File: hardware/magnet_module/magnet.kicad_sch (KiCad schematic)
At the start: 5 parts, among them U2 Leaf_Logo

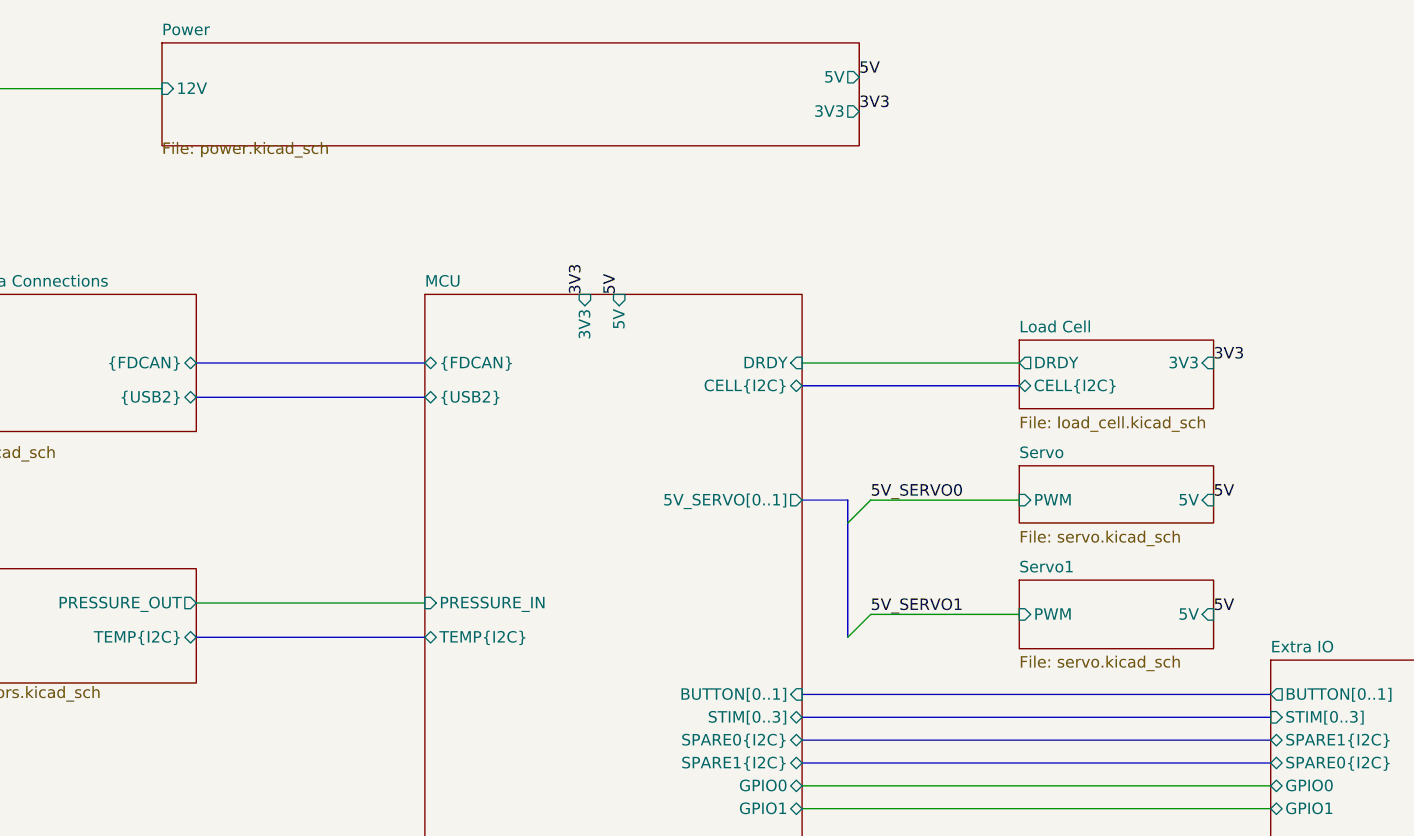
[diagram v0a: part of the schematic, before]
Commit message: change power LED brightness, move level shifter to servo page
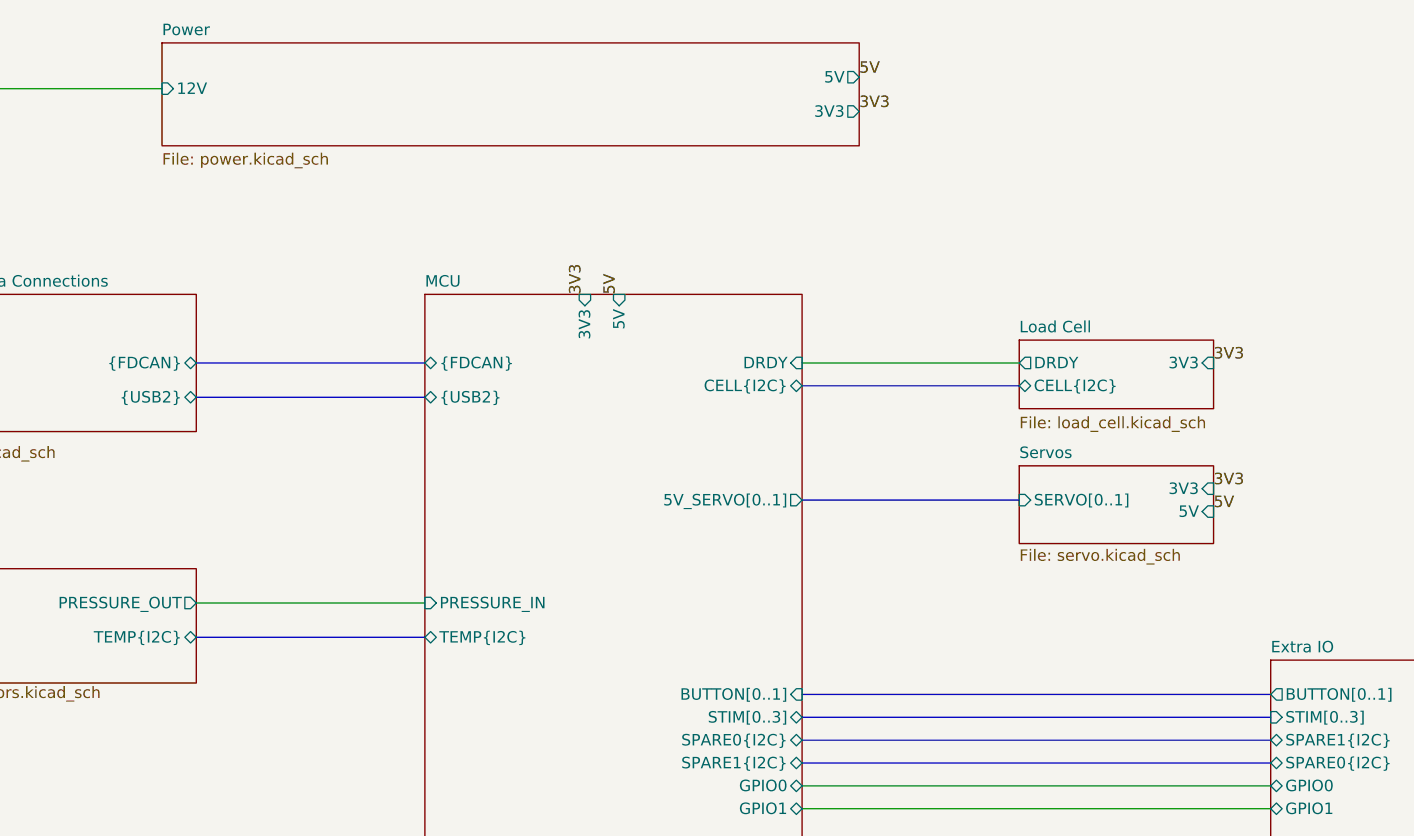
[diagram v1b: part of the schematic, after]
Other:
- sheet Servo renamed Servos
- removed sheet Servo1
- sheet Servos ports: added 3V3, SERVO[0..1]; removed PWM
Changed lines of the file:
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@@
 		(comment 1 "Prepared by LeafLabs, LLC")
 	)
-	(bus_entry
-		(at 176.53 104.14)
-		(size -2.54 2.54)
-		(stroke
-			(width 0)
-			(type default)
-		)
-	)
-	(bus_entry
-		(at 176.53 91.44)
-		(size -2.54 2.54)
+	(bus
+		(pts
+			(xy 168.91 91.44) (xy 193.04 91.44)
+		)
 		(stroke
 			(width 0)
@@
 	(bus
 		(pts
-			(xy 173.99 93.98) (xy 173.99 106.68)
+			(xy 168.91 113.03) (xy 220.98 113.03)
+		)
+		(stroke
+			(width 0)
+			(type default)
+		)
+	)
+	(bus
+		(pts
+			(xy 168.91 120.65) (xy 220.98 120.65)
 		)
 		(stroke
@@
 	(wire
 		(pts
-			(xy 176.53 104.14) (xy 193.04 104.14)
+			(xy 168.91 125.73) (xy 220.98 125.73)
 		)
 		(stroke
@@
 	(bus
 		(pts
-			(xy 168.91 113.03) (xy 220.98 113.03)
+			(xy 168.91 78.74) (xy 193.04 78.74)
+		)
+		(stroke
+			(width 0)
+			(type default)
+		)
+	)
+	(wire
+		(pts
+			(xy 36.83 176.53) (xy 34.29 176.53)
 		)
 		(stroke
@@
 	(bus
 		(pts
-			(xy 168.91 120.65) (xy 220.98 120.65)
+			(xy 168.91 118.11) (xy 220.98 118.11)
 		)
 		(stroke
@@
 	(wire
 		(pts
-			(xy 168.91 125.73) (xy 220.98 125.73)
+			(xy 68.58 72.39) (xy 60.96 72.39)
+		)
+		(stroke
+			(width 0)
+			(type default)
+		)
+	)
+	(wire
+		(pts
+			(xy 168.91 123.19) (xy 220.98 123.19)
+		)
+		(stroke
+			(width 0)
+			(type default)
+		)
+	)
+	(wire
+		(pts
+			(xy 60.96 45.72) (xy 97.79 45.72)
 		)
 		(stroke
@@
 	(bus
 		(pts
-			(xy 168.91 78.74) (xy 193.04 78.74)
-		)
-		(stroke
-			(width 0)
-			(type default)
-		)
-	)
-	(wire
-		(pts
-			(xy 36.83 176.53) (xy 34.29 176.53)
-		)
-		(stroke
-			(width 0)
-			(type default)
-		)
-	)
-	(bus
-		(pts
-			(xy 168.91 118.11) (xy 220.98 118.11)
-		)
-		(stroke
-			(width 0)
-			(type default)
-		)
-	)
-	(wire
-		(pts
-			(xy 68.58 72.39) (xy 60.96 72.39)
-		)
-		(stroke
-			(width 0)
-			(type default)
-		)
-	)
-	(bus
-		(pts
-			(xy 173.99 91.44) (xy 173.99 93.98)
-		)
-		(stroke
-			(width 0)
-			(type default)
-		)
-	)
-	(wire
-		(pts
-			(xy 168.91 123.19) (xy 220.98 123.19)
-		)
-		(stroke
-			(width 0)
-			(type default)
-		)
-	)
-	(wire
-		(pts
-			(xy 60.96 45.72) (xy 97.79 45.72)
-		)
-		(stroke
-			(width 0)
-			(type default)
-		)
-	)
-	(bus
-		(pts
-			(xy 168.91 91.44) (xy 173.99 91.44)
-		)
-		(stroke
-			(width 0)
-			(type default)
-		)
-	)
-	(bus
-		(pts
 			(xy 101.6 76.2) (xy 127 76.2)
-		)
-		(stroke
-			(width 0)
-			(type default)
-		)
-	)
-	(wire
-		(pts
-			(xy 176.53 91.44) (xy 193.04 91.44)
 		)
 		(stroke
@@
 		)
 	)
-	(label "5V_SERVO0"
-		(at 176.53 91.44 0)
+	(label "5V"
+		(at 214.63 92.71 0)
 		(fields_autoplaced yes)
 		(effects
@@
 		)
 	)
-	(label "5V"
-		(at 214.63 91.44 0)
+	(label "3V3"
+		(at 214.63 76.2 0)
 		(fields_autoplaced yes)
 		(effects
@@
 		)
 	)
-	(label "3V3"
-		(at 214.63 76.2 0)
+	(label "5V"
+		(at 175.26 44.45 0)
 		(fields_autoplaced yes)
 		(effects
@@
 		)
 	)
-	(label "5V"
-		(at 175.26 44.45 0)
+	(label "3V3"
+		(at 144.78 68.58 90)
 		(fields_autoplaced yes)
 		(effects
@@
 	)
 	(label "3V3"
-		(at 144.78 68.58 90)
+		(at 214.63 90.17 0)
 		(fields_autoplaced yes)
 		(effects
@@
 		)
 	)
-	(label "5V_SERVO1"
-		(at 176.53 104.14 0)
+	(label "3V3"
+		(at 71.12 101.6 180)
 		(fields_autoplaced yes)
 		(effects
@@
 				(size 1.27 1.27)
 			)
-			(justify left bottom)
-		)
-	)
-	(label "3V3"
-		(at 71.12 101.6 180)
-		(fields_autoplaced yes)
-		(effects
-			(font
-				(size 1.27 1.27)
-			)
 			(justify right bottom)
-		)
-	)
-	(label "5V"
-		(at 214.63 104.14 0)
-		(fields_autoplaced yes)
-		(effects
-			(font
-				(size 1.27 1.27)
-			)
-			(justify left bottom)
 		)
 	)
@@
 		(at 97.79 40.64)
 		(size 77.47 11.43)
-		(fields_autoplaced yes)
 		(stroke
 			(width 0.1524)
@@
 		)
 		(property "Sheetfile" "power.kicad_sch"
-			(at 97.79 51.6386 0)
+			(at 97.79 52.832 0)
 			(effects
 				(font
@@
 	(sheet
 		(at 193.04 87.63)
-		(size 21.59 6.35)
+		(size 21.59 8.636)
 		(fields_autoplaced yes)
 		(stroke
@@
 			(color 0 0 0 0.0000)
 		)
-		(property "Sheetname" "Servo"
+		(property "Sheetname" "Servos"
 			(at 193.04 86.9184 0)
 			(effects
@@
 		)
 		(property "Sheetfile" "servo.kicad_sch"
-			(at 193.04 94.8186 0)
+			(at 193.04 96.8506 0)
 			(effects
 				(font
@@
 		)
 		(pin "5V" input
-			(at 214.63 91.44 0)
-			(effects
-				(font
-					(size 1.27 1.27)
-				)
-				(justify right)
-			)
-		)
-		(pin "PWM" input
+			(at 214.63 92.71 0)
+			(effects
+				(font
+					(size 1.27 1.27)
+				)
+				(justify right)
+			)
+		)
+		(pin "3V3" input
+			(at 214.63 90.17 0)
+			(effects
+				(font
+					(size 1.27 1.27)
+				)
+				(justify right)
+			)
+		)
+		(pin "SERVO[0..1]" input
 			(at 193.04 91.44 180)
 			(effects
@@
 				)
 			)
-		)
-	)
-	(sheet
-		(at 193.04 100.33)
-		(size 21.59 7.62)
-		(stroke
-			(width 0.1524)
-			(type solid)
-		)
-		(fill
-			(color 0 0 0 0.0000)
-		)
-		(property "Sheetname" "Servo1"
-			(at 193.04 99.6184 0)
-			(effects
-				(font
-					(size 1.27 1.27)
-				)
-				(justify left bottom)
-			)
-		)
-		(property "Sheetfile" "servo.kicad_sch"
-			(at 193.04 108.712 0)
-			(effects
-				(font
-					(size 1.27 1.27)
-				)
-				(justify left top)
-			)
-		)
-		(pin "5V" input
-			(at 214.63 104.14 0)
-			(effects
-				(font
-					(size 1.27 1.27)
-				)
-				(justify right)
-			)
-		)
-		(pin "PWM" input
-			(at 193.04 104.14 180)
-			(effects
-				(font
-					(size 1.27 1.27)
-				)
-				(justify left)
-			)
-		)
-		(instances
-			(project "magnet"
-				(path "/aa5044b8-67cd-4b5a-a593-0df9431eb095"
-					(page "5")
-				)
-			)

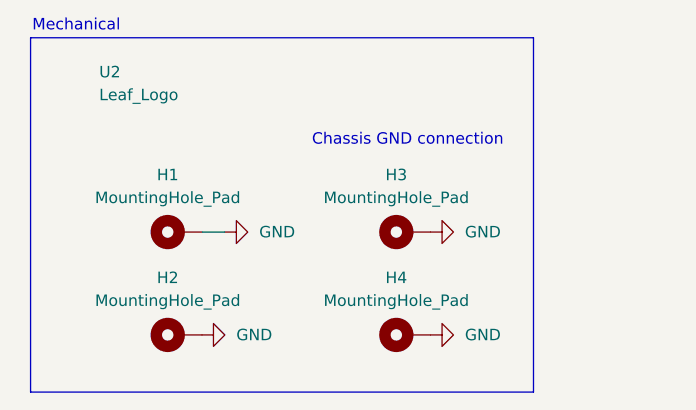
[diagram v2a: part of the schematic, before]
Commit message: add all PNs, relevant datasheets, and test points
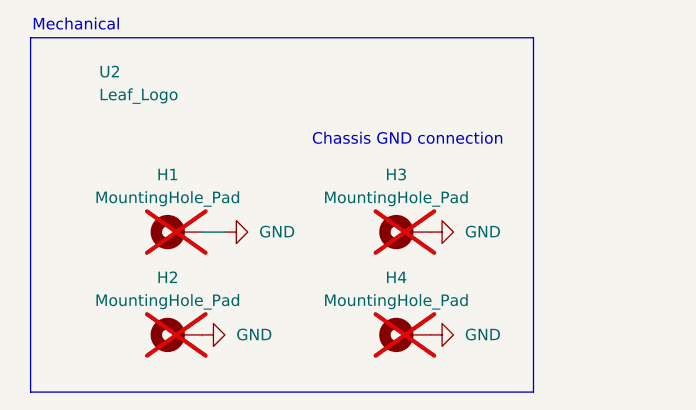
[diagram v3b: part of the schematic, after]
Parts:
- H1, H2, H3, H4, U2: now not fitted
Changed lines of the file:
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@@
 		(in_bom no)
 		(on_board yes)
-		(dnp no)
+		(dnp yes)
 		(fields_autoplaced yes)
 		(property "Reference" "H4"
@@
 		(in_bom no)
 		(on_board yes)
-		(dnp no)
+		(dnp yes)
 		(fields_autoplaced yes)
 		(property "Reference" "H3"
@@
 		(in_bom no)
 		(on_board yes)
-		(dnp no)
+		(dnp yes)
 		(fields_autoplaced yes)
 		(property "Reference" "H2"
@@
 		(in_bom no)
 		(on_board yes)
-		(dnp no)
+		(dnp yes)
 		(fields_autoplaced yes)
 		(property "Reference" "U2"
@@
 		(in_bom no)
 		(on_board yes)
-		(dnp no)
+		(dnp yes)
 		(fields_autoplaced yes)
 		(property "Reference" "H1"

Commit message: make changes as requested by Ryan
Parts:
- H1, H2, H3, H4, U2: now fitted
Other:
- sheet Extra IO ports: added none; removed STIM[0..3]
- sheet MCU ports: added none; removed STIM[0..3]
- company: Christie Lab, CU-Anschultz -> Christie Lab, CU-Anschutz
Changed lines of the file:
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@@
 		(date "2024-07-09")
 		(rev "v1.0")
-		(company "Christie Lab, CU-Anschultz")
+		(company "Christie Lab, CU-Anschutz")
 		(comment 1 "Prepared by LeafLabs, LLC")
 	)
@@
 		(pts
 			(xy 168.91 76.2) (xy 193.04 76.2)
-		)
-		(stroke
-			(width 0)
-			(type default)
-		)
-	)
-	(bus
-		(pts
-			(xy 168.91 115.57) (xy 220.98 115.57)
 		)
 		(stroke
@@
 		(in_bom no)
 		(on_board yes)
-		(dnp yes)
+		(dnp no)
 		(fields_autoplaced yes)
 		(property "Reference" "H4"
@@
 		(in_bom no)
 		(on_board yes)
-		(dnp yes)
+		(dnp no)
 		(fields_autoplaced yes)
 		(property "Reference" "H3"
@@
 		(in_bom no)
 		(on_board yes)
-		(dnp yes)
+		(dnp no)
 		(fields_autoplaced yes)
 		(property "Reference" "H2"
@@
 		(in_bom no)
 		(on_board yes)
-		(dnp yes)
+		(dnp no)
 		(fields_autoplaced yes)
 		(property "Reference" "U2"
@@
 		(in_bom no)
 		(on_board yes)
-		(dnp yes)
+		(dnp no)
 		(fields_autoplaced yes)
 		(property "Reference" "H1"
@@
 			)
 		)
-		(pin "STIM[0..3]" bidirectional
-			(at 168.91 115.57 0)
-			(effects
-				(font
-					(size 1.27 1.27)
-				)
-				(justify right)
-			)
-		)
 		(pin "SPARE0{I2C}" bidirectional
 			(at 168.91 118.11 0)
@@
 			)
 		)
-		(pin "STIM[0..3]" input
-			(at 220.98 115.57 180)
-			(effects
-				(font
-					(size 1.27 1.27)
-				)
-				(justify left)
-			)
-		)

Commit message: make changes requested by dan, run ERC
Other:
- sheet Extra IO ports: added none; removed 5V
- sheet MCU ports: added SERVO[0..1]; removed 5V, 5V_SERVO[0..1]
- sheet Sensors ports: added PRESSURE_FILT; removed PRESSURE_OUT
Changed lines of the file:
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@@
-	)
-	(label "5V"
-		(at 148.59 68.58 90)
-		(fields_autoplaced yes)
-		(effects
-			(font
-				(size 1.27 1.27)
-			)
-			(justify left bottom)
-		)
-	)
-	(label "5V"
-		(at 247.65 114.3 0)
-		(fields_autoplaced yes)
-		(effects
-			(font
-				(size 1.27 1.27)
-			)
-			(justify left bottom)
-		)
 	)
 	(label "5V"
@@
 			)
 		)
-		(pin "5V_SERVO[0..1]" output
-			(at 168.91 91.44 0)
-			(effects
-				(font
-					(size 1.27 1.27)
-				)
-				(justify right)
-			)
-		)
-		(pin "5V" input
-			(at 148.59 68.58 90)
-			(effects
-				(font
-					(size 1.27 1.27)
-				)
-				(justify right)
-			)
-		)
 		(pin "BUTTON[0..1]" input
 			(at 168.91 113.03 0)
@@
 		(pin "GPIO1" bidirectional
 			(at 168.91 125.73 0)
+			(effects
+				(font
+					(size 1.27 1.27)
+				)
+				(justify right)
+			)
+		)
+		(pin "SERVO[0..1]" output
+			(at 168.91 91.44 0)
 			(effects
 				(font
@@
 			)
 		)
-		(pin "PRESSURE_OUT" output
-			(at 101.6 102.87 0)
-			(effects
-				(font
-					(size 1.27 1.27)
-				)
-				(justify right)
-			)
-		)
 		(pin "TEMP{I2C}" bidirectional
 			(at 101.6 106.68 0)
+			(effects
+				(font
+					(size 1.27 1.27)
+				)
+				(justify right)
+			)
+		)
+		(pin "PRESSURE_FILT" output
+			(at 101.6 102.87 0)
 			(effects
 				(font
@@
 			)
 		)
-		(pin "5V" input
-			(at 247.65 114.3 0)
-			(effects
-				(font
-					(size 1.27 1.27)
-				)
-				(justify right)
-			)
-		)

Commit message: add footprints & 3d models for magnet module connector placmeent
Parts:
- H1, H2, H3, H4: footprint (none) -> MountingHole:MountingHole_3.2mm_M3_Pad
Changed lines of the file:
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@@
 			)
 		)
-		(property "Footprint" ""
+		(property "Footprint" "MountingHole:MountingHole_3.2mm_M3_Pad"
 			(at 57.15 187.96 0)
 			(effects
@@
 			)
 		)
-		(property "Footprint" ""
+		(property "Footprint" "MountingHole:MountingHole_3.2mm_M3_Pad"
 			(at 57.15 176.53 0)
 			(effects
@@
 			)
 		)
-		(property "Footprint" ""
+		(property "Footprint" "MountingHole:MountingHole_3.2mm_M3_Pad"
 			(at 31.75 187.96 0)
 			(effects
@@
 			)
 		)
-		(property "Footprint" ""
+		(property "Footprint" "MountingHole:MountingHole_3.2mm_M3_Pad"
 			(at 31.75 176.53 0)
 			(effects

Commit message: Schematic updates to remove button connectors and extra STEMMA QT
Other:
- sheet Extra IO ports: added none; removed BUTTON[0..1], SPARE1{I2C}
- sheet MCU ports: added none; removed BUTTON[0..1], SPARE1{I2C}
- sheet Sensors ports: added 5V; removed none
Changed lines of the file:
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@@
+		)
+	)
+	(wire
+		(pts
+			(xy 168.91 125.73) (xy 220.98 125.73)
+		)
+		(stroke
+			(width 0)
+			(type default)
 		)
 	)
 	(bus
 		(pts
-			(xy 168.91 113.03) (xy 220.98 113.03)
+			(xy 168.91 78.74) (xy 193.04 78.74)
+		)
+		(stroke
+			(width 0)
+			(type default)
+		)
+	)
+	(wire
+		(pts
+			(xy 36.83 176.53) (xy 34.29 176.53)
 		)
 		(stroke
@@
 		(pts
 			(xy 168.91 120.65) (xy 220.98 120.65)
-		)
-		(stroke
-			(width 0)
-			(type default)
-		)
-	)
-	(wire
-		(pts
-			(xy 168.91 125.73) (xy 220.98 125.73)
-		)
-		(stroke
-			(width 0)
-			(type default)
-		)
-	)
-	(bus
-		(pts
-			(xy 168.91 78.74) (xy 193.04 78.74)
-		)
-		(stroke
-			(width 0)
-			(type default)
-		)
-	)
-	(wire
-		(pts
-			(xy 36.83 176.53) (xy 34.29 176.53)
-		)
-		(stroke
-			(width 0)
-			(type default)
-		)
-	)
-	(bus
-		(pts
-			(xy 168.91 118.11) (xy 220.98 118.11)
 		)
 		(stroke
@@
 	(label "3V3"
 		(at 71.12 101.6 180)
+		(fields_autoplaced yes)
+		(effects
+			(font
+				(size 1.27 1.27)
+			)
+			(justify right bottom)
+		)
+	)
+	(label "5V"
+		(at 71.12 104.14 180)
 		(fields_autoplaced yes)
 		(effects
@@
 			)
 		)
-		(pin "BUTTON[0..1]" input
-			(at 168.91 113.03 0)
-			(effects
-				(font
-					(size 1.27 1.27)
-				)
-				(justify right)
-			)
-		)
 		(pin "SPARE0{I2C}" bidirectional
-			(at 168.91 118.11 0)
-			(effects
-				(font
-					(size 1.27 1.27)
-				)
-				(justify right)
-			)
-		)
-		(pin "SPARE1{I2C}" bidirectional
 			(at 168.91 120.65 0)
 			(effects
@@
 			)
 		)
+		(pin "5V" input
+			(at 71.12 104.14 180)
+			(effects
+				(font
+					(size 1.27 1.27)
+				)
+				(justify left)
+			)
+		)
 		(instances
 			(project "magnet"
@@
 			)
 		)
-		(pin "BUTTON[0..1]" output
-			(at 220.98 113.03 180)
-			(effects
-				(font
-					(size 1.27 1.27)
-				)
-				(justify left)
-			)
-		)
 		(pin "3V3" input
 			(at 247.65 118.11 0)
@@
 			)
 		)
-		(pin "SPARE1{I2C}" bidirectional
-			(at 220.98 118.11 180)
-			(effects
-				(font
-					(size 1.27 1.27)
-				)
-				(justify left)
-			)
-		)
